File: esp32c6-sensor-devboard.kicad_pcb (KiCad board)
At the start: 4 copper layers, 90 x 50 mm, 193 parts, among them J1 Conn_01x04_Pin, J2 Micro_SD_Card_Det1, J3 Screw_Terminal_01x02, J4 USB_C_Receptacle_USB2.0_14P, J5 Screw_Terminal_01x02, J6 Screw_Terminal_01x06, J7 Screw_Terminal_01x04, J8 Conn_01x04_Pin, J9 Conn_01x03_Pin, SW1 SW_Push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

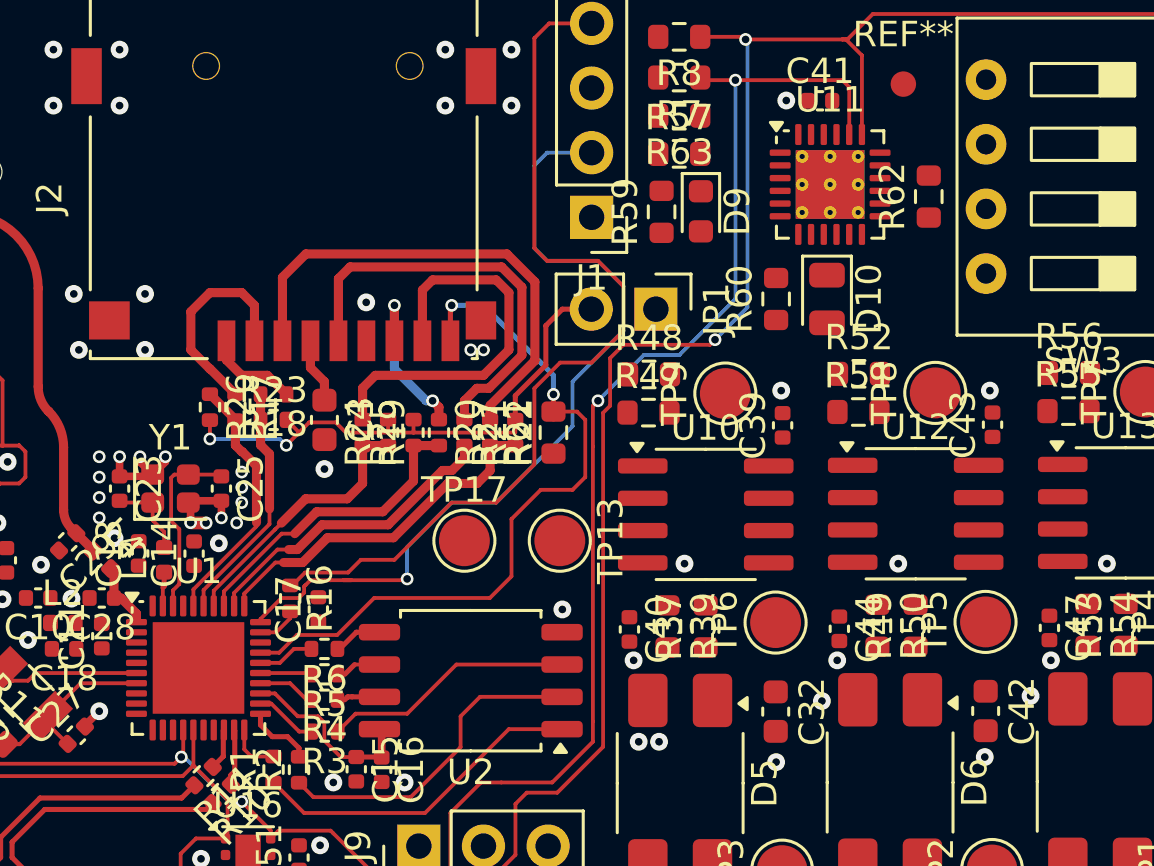
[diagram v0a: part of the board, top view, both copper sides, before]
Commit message: pcb: increase footprints via sizes
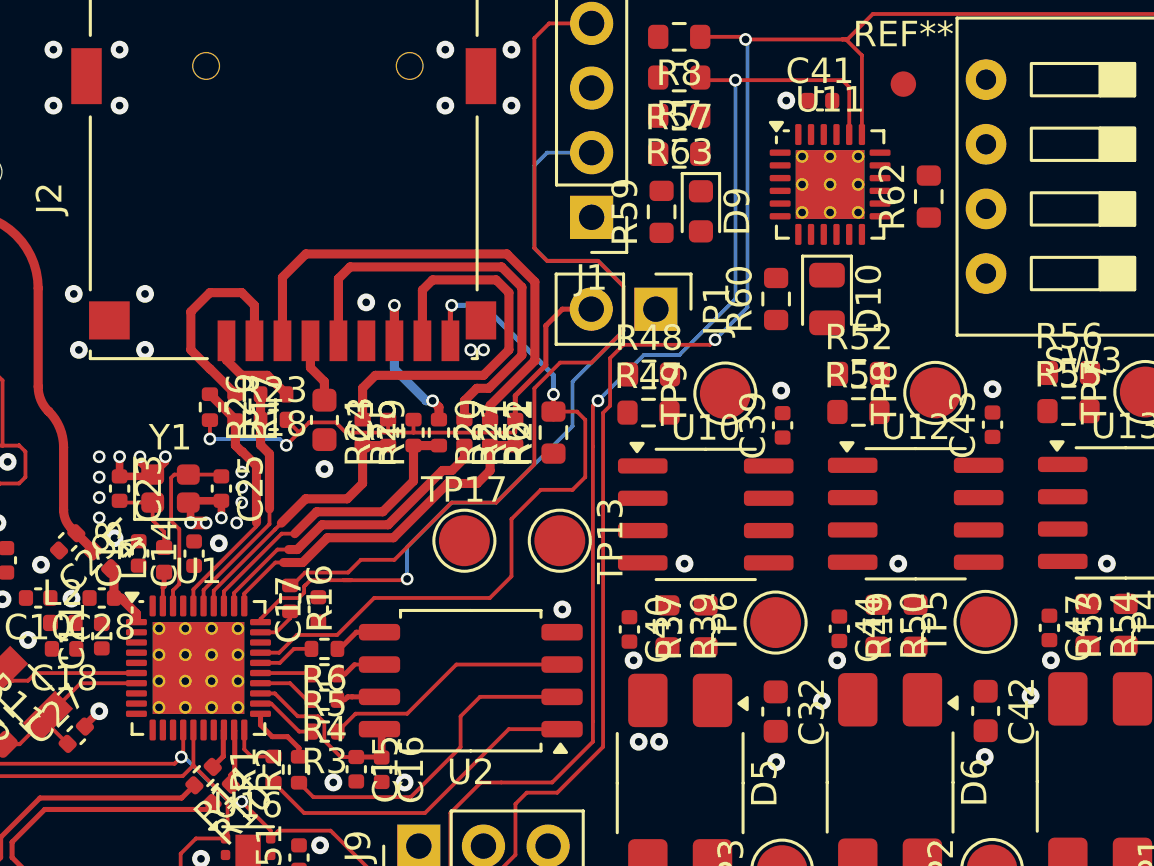
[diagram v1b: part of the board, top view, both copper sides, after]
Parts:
- U1: footprint Package_DFN_QFN:QFN-40-1EP_5x5mm_P0.4mm_EP3.6x3.6mm -> Package_DFN_QFN:QFN-40-1EP_5x5mm_P0.4mm_EP3.6x3.6mm_ThermalVias

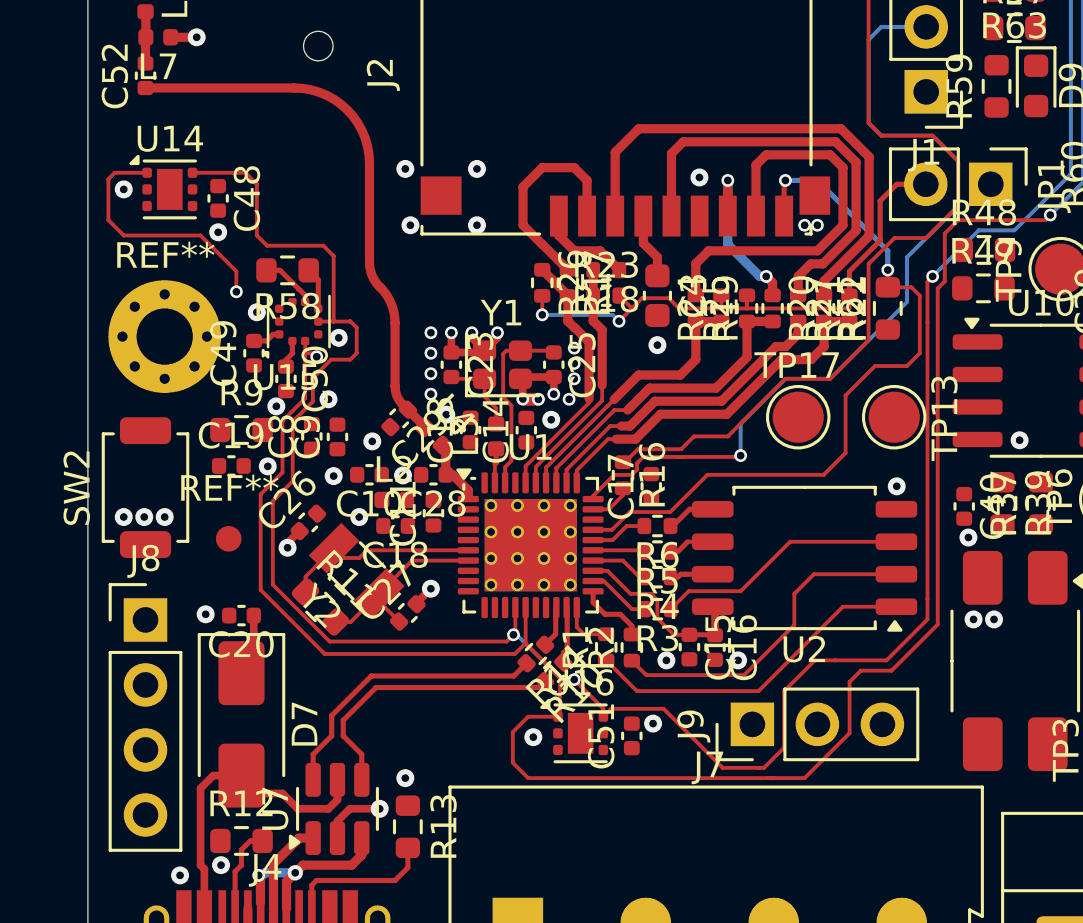
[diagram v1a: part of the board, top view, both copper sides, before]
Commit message: pcb: add TMP1117 temps routing
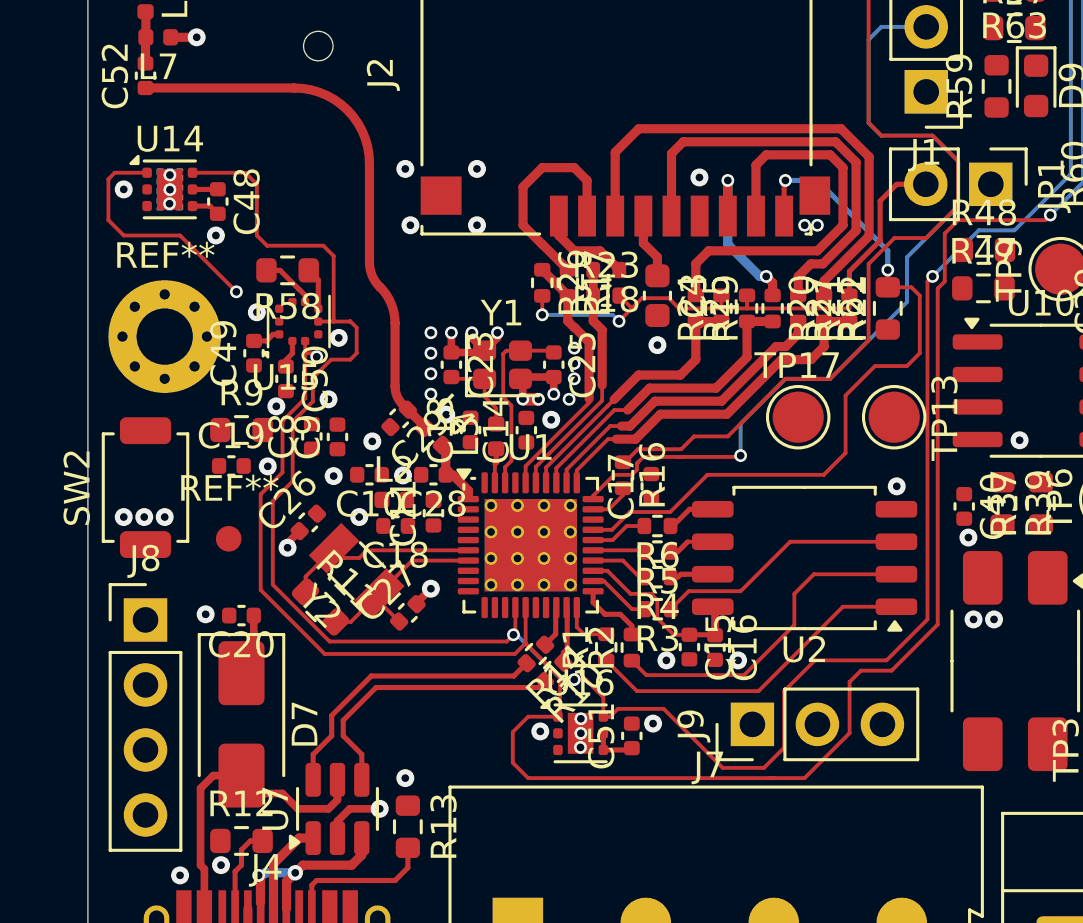
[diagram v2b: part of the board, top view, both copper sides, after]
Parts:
- moved C48 0.12 mm to (137.1, 81.1)
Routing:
- net +3V3: track 6.94 -> 9.72 mm
- net GND: track 12.8 -> 13.9 mm, vias 111 -> 117
- added copper zone on B.Cu, net GND

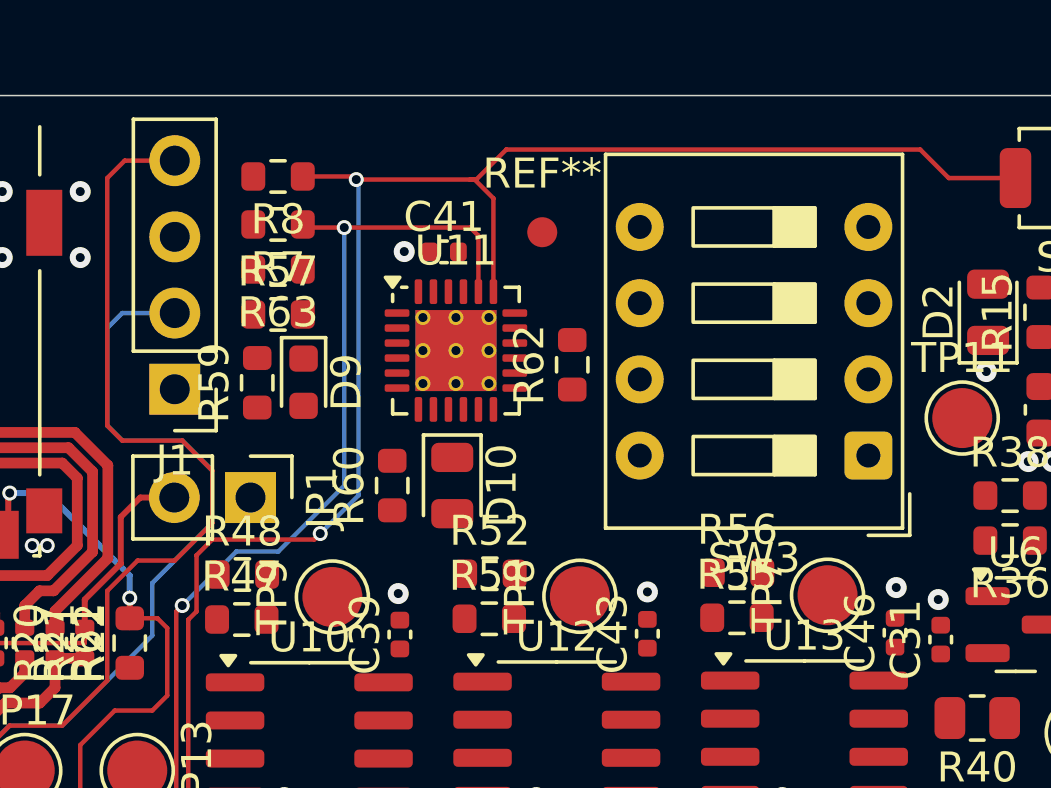
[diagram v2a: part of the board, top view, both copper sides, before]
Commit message: pcb: add TCA9555 routing
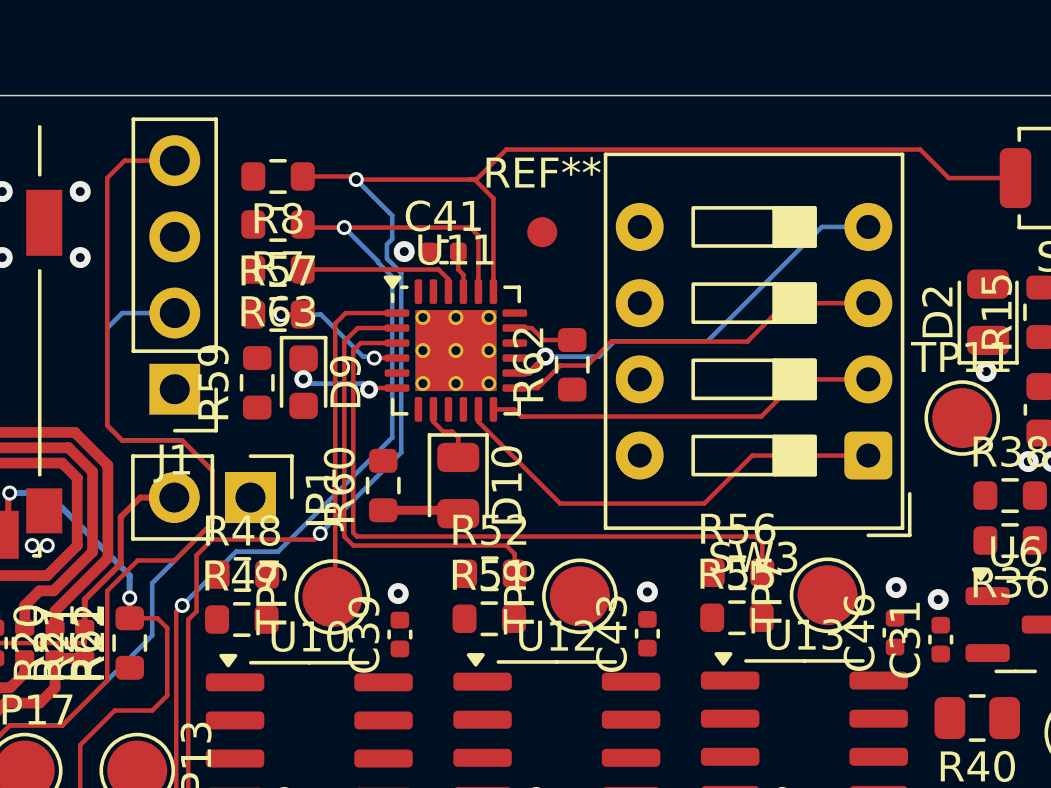
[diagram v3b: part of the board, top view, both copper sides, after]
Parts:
- moved R60 0.30 mm to (171.7, 80.0)
- moved D10 0.20 mm to (174.2, 80.0)
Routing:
- net /IL3: track 0.00 -> 22.4 mm
- net Net-(U11-P11): track 0.00 -> 15.2 mm
- net /IL2: track 0.00 -> 15.0 mm
- net Net-(U11-P14): track 0.00 -> 13.8 mm, vias 0 -> 1
- net Net-(U11-P12): track 0.00 -> 13.1 mm
- net Net-(U11-P13): track 0.00 -> 13.0 mm
- net /IL1: track 0.00 -> 11.4 mm
- net Net-(U1-GPIO10): track 0.00 -> 5.40 mm
- net /TMP117_ALERT: track 0.00 -> 5.18 mm, vias 0 -> 2
- net Net-(D9-K): track 0.00 -> 3.98 mm, vias 0 -> 2
- net Net-(D10-A): track 0.00 -> 2.55 mm
- net Net-(D10-K): track 0.00 -> 2.12 mm
- net /TMP117_ALERT2: track 0.00 -> 2.08 mm
- net +3V3: track 9.72 -> 11.1 mm
- net /BOOT/SCL: track 126.8 -> 128.2 mm
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
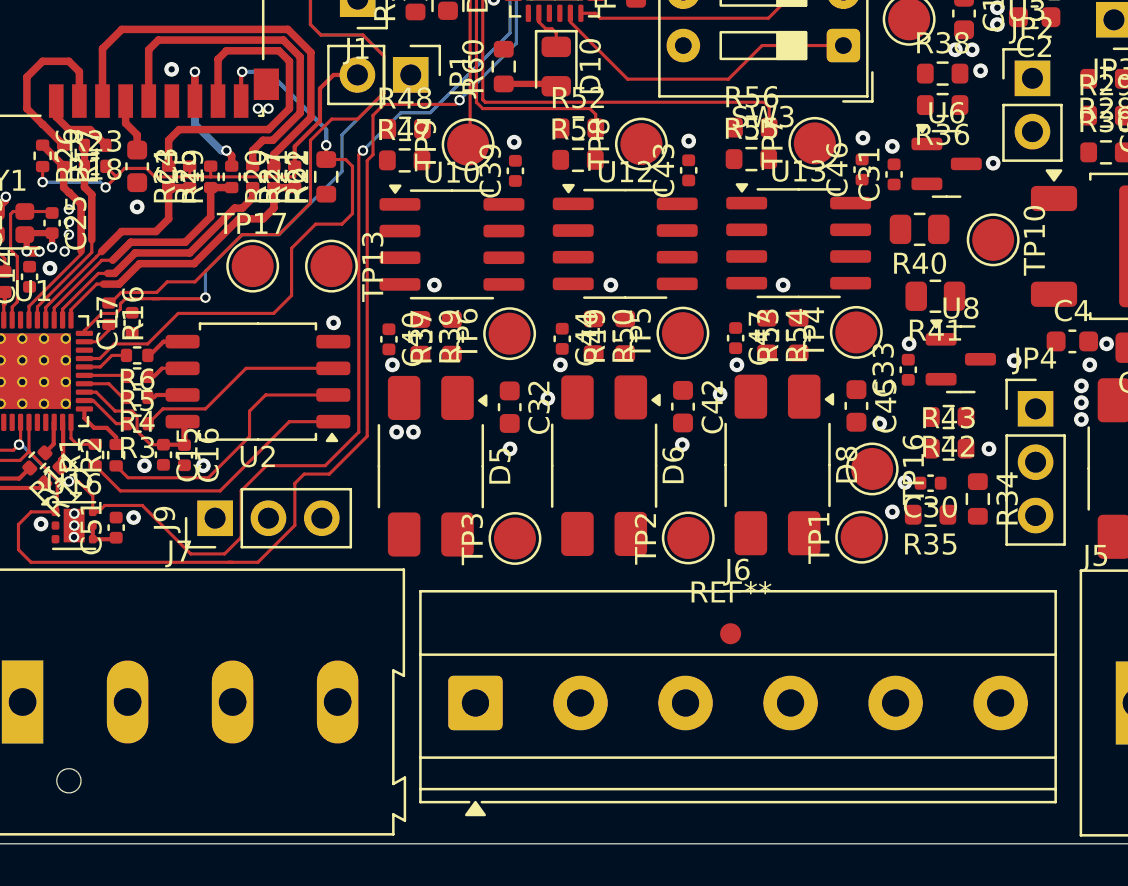
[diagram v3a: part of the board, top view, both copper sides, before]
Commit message: pcb: add level shifter routing
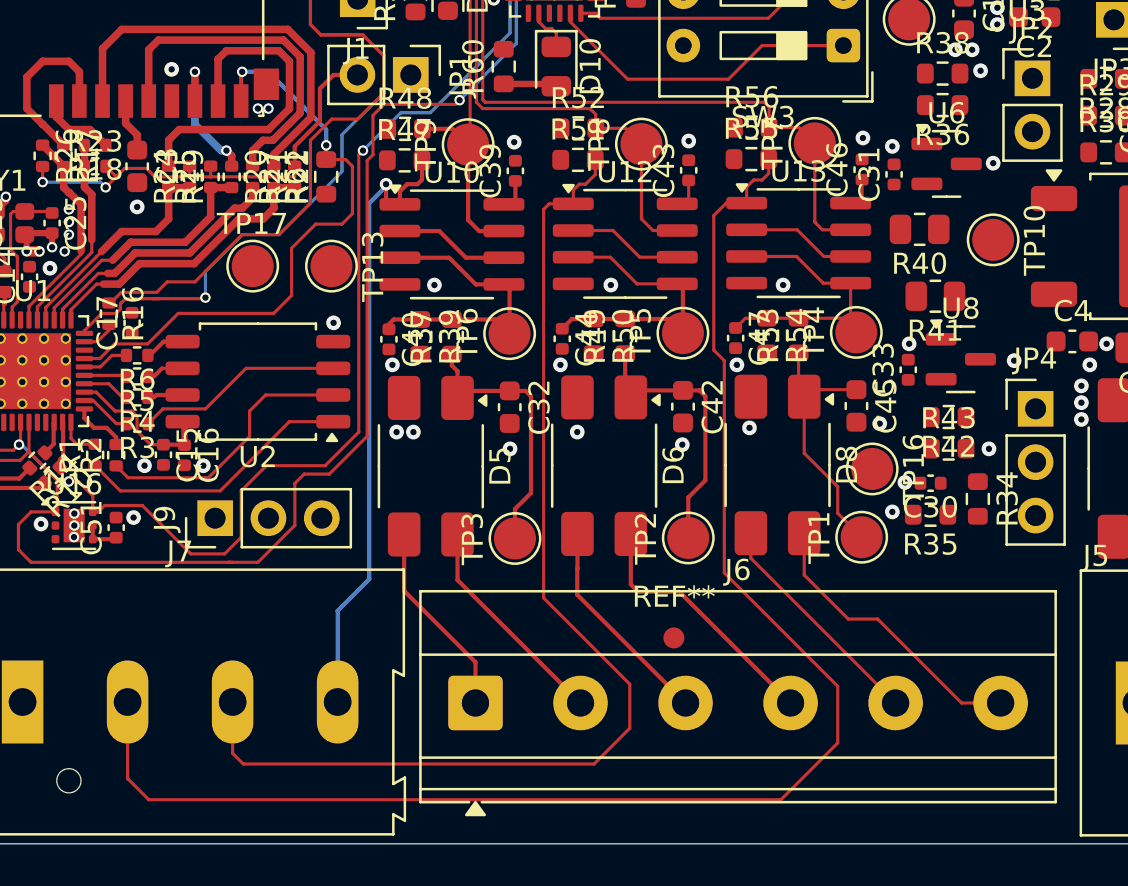
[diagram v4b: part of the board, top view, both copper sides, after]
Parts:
- moved REF** 2.71 mm to (179.8, 107.2)
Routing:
- net /I3: track 0.00 -> 71.1 mm
- net /I2: track 0.00 -> 52.9 mm
- net /I1: track 0.00 -> 29.3 mm, vias 0 -> 1
- net /Vref: track 0.00 -> 16.4 mm
- net Net-(U10A-+): track 0.00 -> 14.3 mm
- net Net-(U13A-+): track 0.00 -> 14.2 mm
- net Net-(U12A-+): track 0.00 -> 14.2 mm
- net /AC Level Shifter/I1: track 0.00 -> 13.9 mm
- net Net-(C42-Pad1): track 0.00 -> 13.1 mm
- net Net-(C32-Pad1): track 0.00 -> 13.0 mm
- net Net-(C45-Pad1): track 0.00 -> 12.6 mm
- net /AC Level Shifter1/I1: track 0.00 -> 12.3 mm
- net /AC Level Shifter/I2: track 0.00 -> 10.9 mm
- net /AC Level Shifter2/I1: track 0.00 -> 10.4 mm
- net /AC Level Shifter1/I2: track 0.00 -> 10.2 mm
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
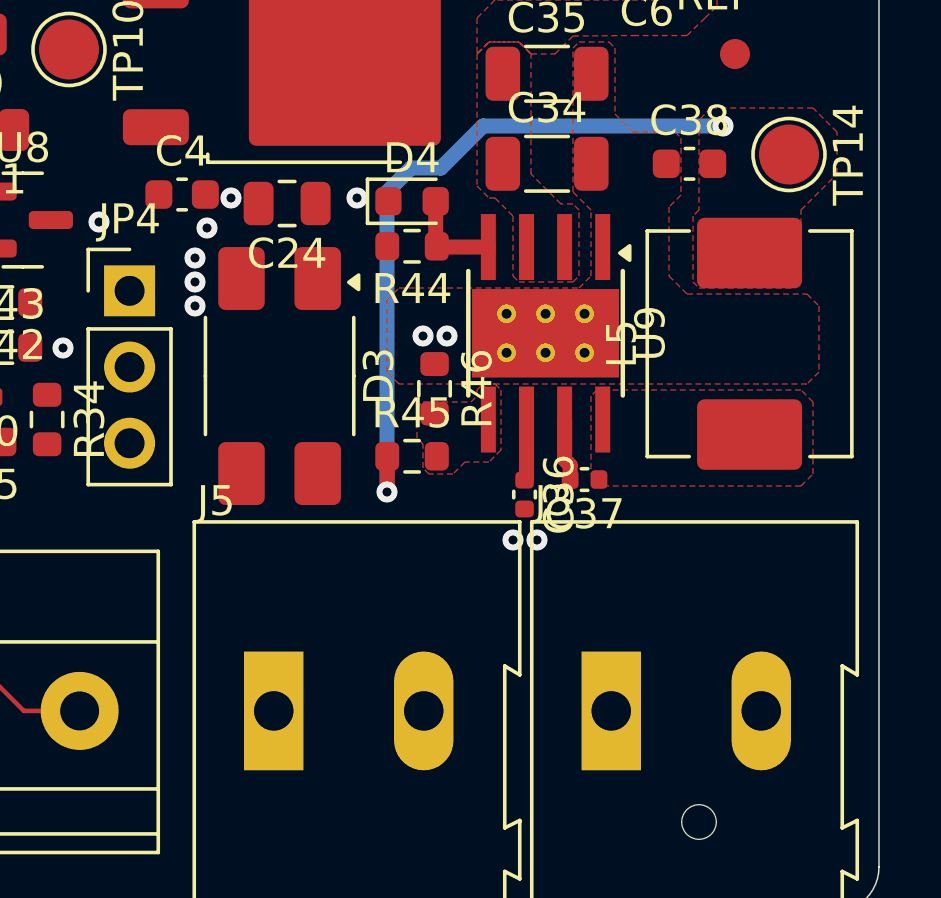
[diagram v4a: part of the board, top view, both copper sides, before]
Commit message: pcb: power rectifier routing
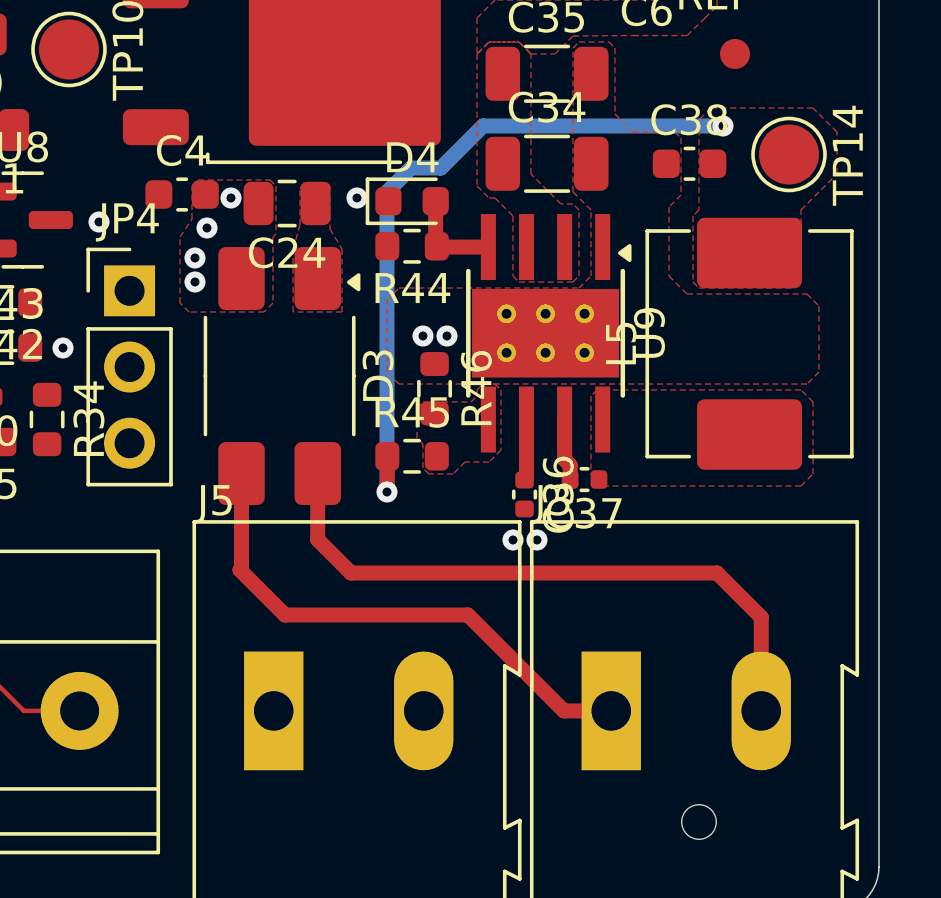
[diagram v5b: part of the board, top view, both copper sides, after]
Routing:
- net /Power/-12/24AC: track 0.00 -> 21.2 mm
- net /Power/+12/24AC: track 0.00 -> 17.6 mm
- net GND: vias 117 -> 116
